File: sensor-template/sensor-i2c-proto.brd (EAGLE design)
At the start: 22.1 x 27.3 mm, 19 parts, among them U2 ATMEGA328PB-AUR

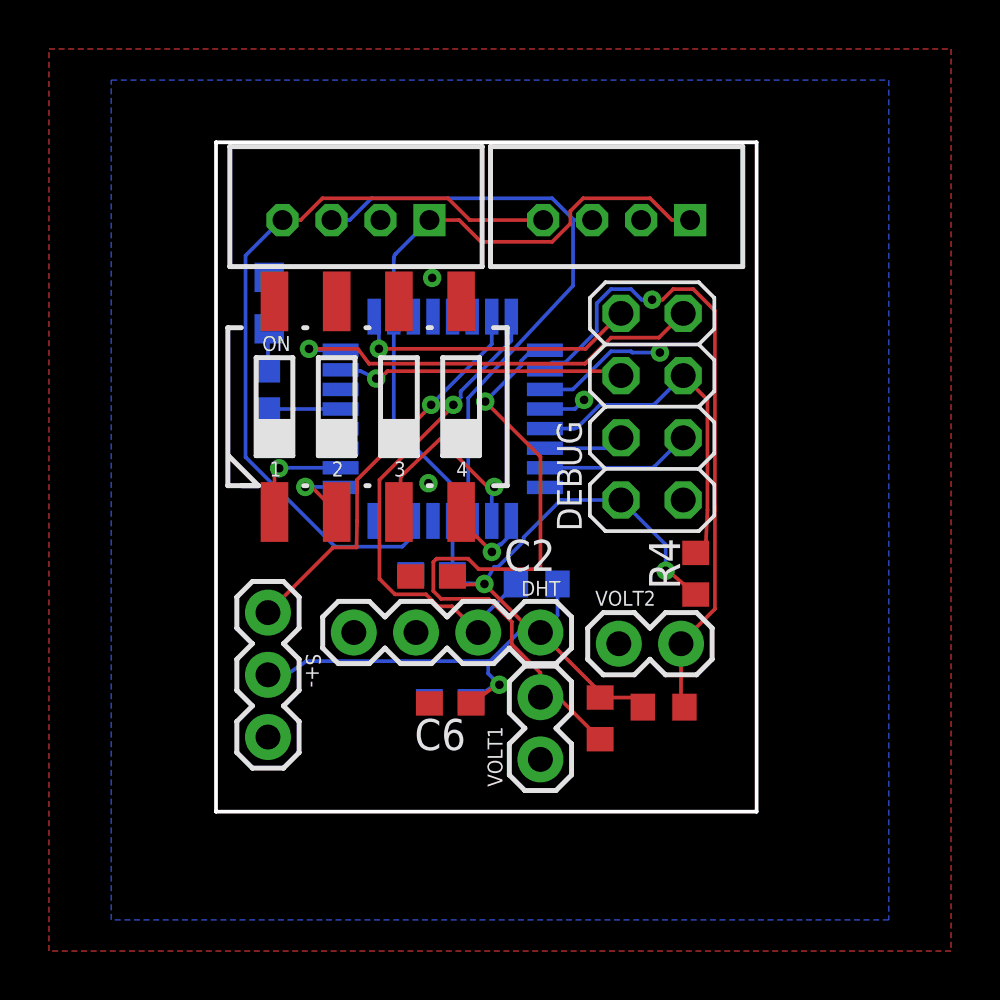
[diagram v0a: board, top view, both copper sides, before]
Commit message: Two sensor examples
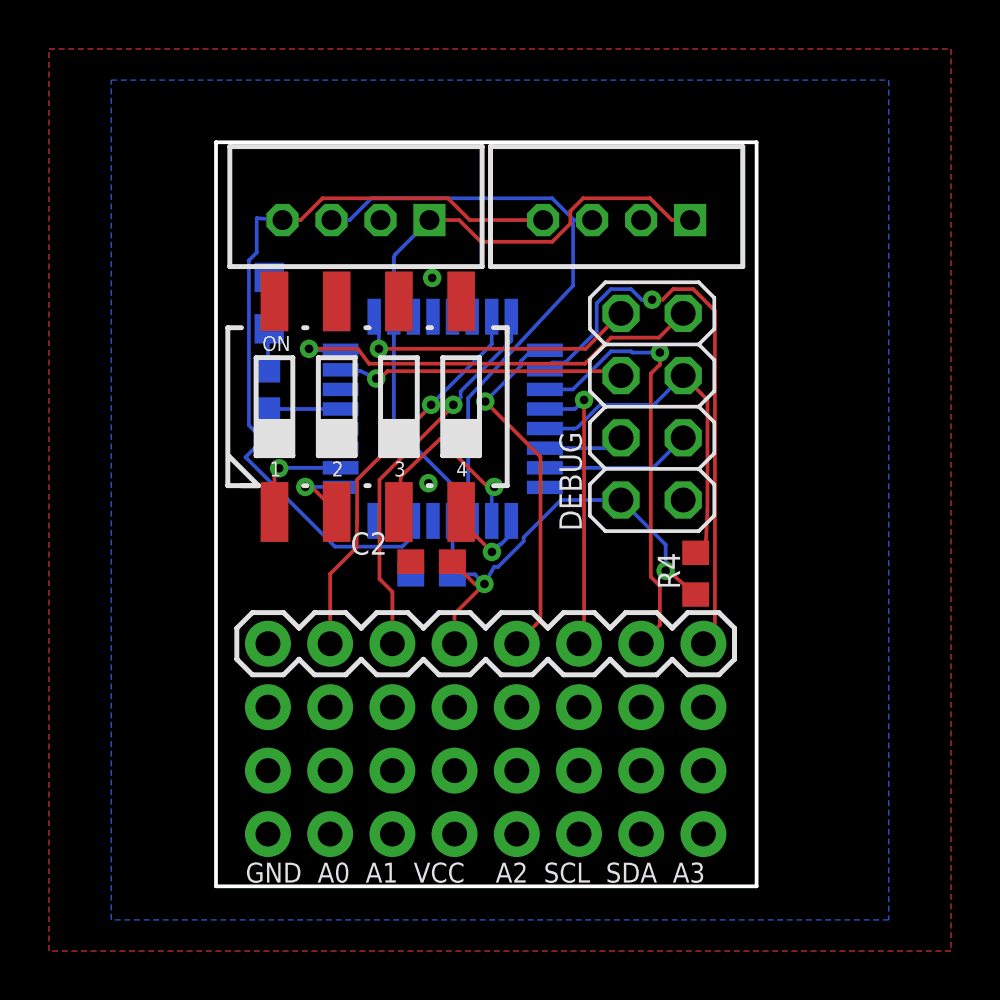
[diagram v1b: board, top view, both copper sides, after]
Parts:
- removed C5: 10u, resistor:C0603
- removed C6: 0.1u, resistor:C0603
- removed DHT: (no value), SparkFun-Connectors:1X04
- removed R1: 4.7k, resistor:R0603
- removed R2, R3: (no value), resistor:R0603
- removed S+-: (no value), SparkFun-Connectors:1X03
- removed VOLT1, VOLT2: (no value), SparkFun-Connectors:1X02
- added J1: (no value), SparkFun-Connectors:1X08
- added J2, J3, J4: (no value), SparkFun-Connectors:1X08_NO_SILK
- moved C2 0.61 mm to (9.27, 10.8)
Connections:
- removed net N$6: DHT.3
- net A0: now also J1.2; no longer S+-.3
- net A1: now also J1.3; no longer DHT.2, R1.1
- net A2: now also J1.5; no longer R2.1, VOLT1.2
- net A3: now also J1.8; no longer R3.1, VOLT2.2
- net GND: now also J1.1; no longer DHT.4, S+-.1, VOLT1.1, VOLT2.1
- net SCL0: now also J1.6
- net SDA0: now also J1.7
- net VCC: now also J1.4; no longer C5.1, C6.1, DHT.1, R1.2, R2.2, R3.2, S+-.2
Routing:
- net VCC: track 70.8 -> 47.4 mm, vias 3 -> 2
- net A2: track 27.5 -> 14.7 mm
- net SDA0: track 5.36 -> 17.9 mm
- net SCL0: track 1.75 -> 11.8 mm
- net A1: track 20.5 -> 15.8 mm
- net A3: track 26.5 -> 23.5 mm
- net SCL1: track 30.9 -> 31.8 mm
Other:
- board size 22.1 x 27.3 mm -> 22.1 x 30.4 mm
- board text added: "(c) Sunmola Oreoluwa, Jimmy He"
- board text added: "A2 SCL SDA A3"
- board text added: "GND A0 A1 VCC"
- board text added: "Prototyping v0.1"
- board text added: "WaggleNet Sensor"

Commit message: [sensor] Debug connector now complies to node arrangement
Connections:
- net RX0: now also DEBUG.3; no longer DEBUG.4
- net TX0: now also DEBUG.4; no longer DEBUG.3
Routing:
- net RX0: track 3.27 -> 7.00 mm
- net TX0: track 6.14 -> 3.61 mm
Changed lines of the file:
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@@
 <signal name="RX0">
 <contactref element="U2" pad="30"/>
-<contactref element="DEBUG" pad="4"/>
-<wire x1="16.474790625" y1="15.4497" x2="16.65439375" y2="15.52409375" width="0.1524" layer="16" curve="44.999502"/>
-<wire x1="16.65439375" y1="15.52409375" x2="17.0053" y2="15.875" width="0.1524" layer="16"/>
-<wire x1="13.8982" y1="15.4497" x2="16.474790625" y2="15.4497" width="0.1524" layer="16"/>
+<contactref element="DEBUG" pad="3"/>
+<wire x1="19.12" y1="15.4497" x2="19.5453" y2="15.875" width="0.1524" layer="16"/>
+<wire x1="16.594975" y1="16.8656" x2="17.415625" y2="16.8656" width="0.1524" layer="16"/>
+<wire x1="13.8982" y1="15.4497" x2="15.179075" y2="15.4497" width="0.1524" layer="16"/>
+<wire x1="18.831525" y1="15.4497" x2="19.12" y2="15.4497" width="0.1524" layer="16"/>
+<wire x1="15.179075" y1="15.4497" x2="16.594975" y2="16.8656" width="0.1524" layer="16"/>
+<wire x1="17.415625" y1="16.8656" x2="18.831525" y2="15.4497" width="0.1524" layer="16"/>
 </signal>
 <signal name="TX0">
 <contactref element="U2" pad="31"/>
-<contactref element="DEBUG" pad="3"/>
-<wire x1="13.8982" y1="14.6497" x2="18.214790625" y2="14.6497" width="0.1524" layer="16"/>
-<wire x1="18.214790625" y1="14.6497" x2="18.39439375" y2="14.72409375" width="0.1524" layer="16" curve="44.999502"/>
-<wire x1="18.39439375" y1="14.72409375" x2="19.5453" y2="15.875" width="0.1524" layer="16"/>
+<contactref element="DEBUG" pad="4"/>
+<wire x1="13.8982" y1="14.6497" x2="15.78" y2="14.6497" width="0.1524" layer="16"/>
+<wire x1="15.78" y1="14.6497" x2="17.0053" y2="15.875" width="0.1524" layer="16"/>
 </signal>
 <signal name="N$1">
